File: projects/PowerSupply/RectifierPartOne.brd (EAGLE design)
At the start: 95 x 75 mm, 16 parts, among them K1 G2R2, X1 LINE-IN, X2 T1-PRI, X3 T1-SEC, X4 R1-OUT

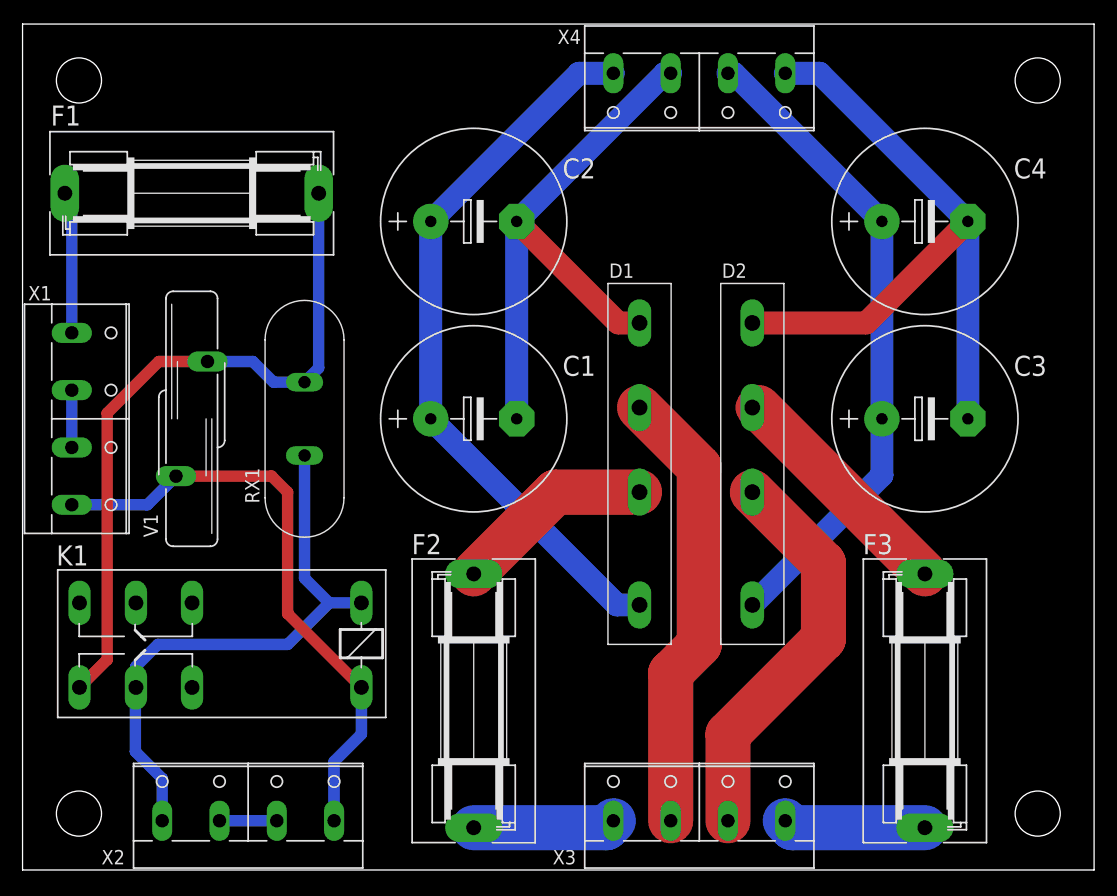
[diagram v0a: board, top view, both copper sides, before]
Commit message: feat: rectifier part one modified
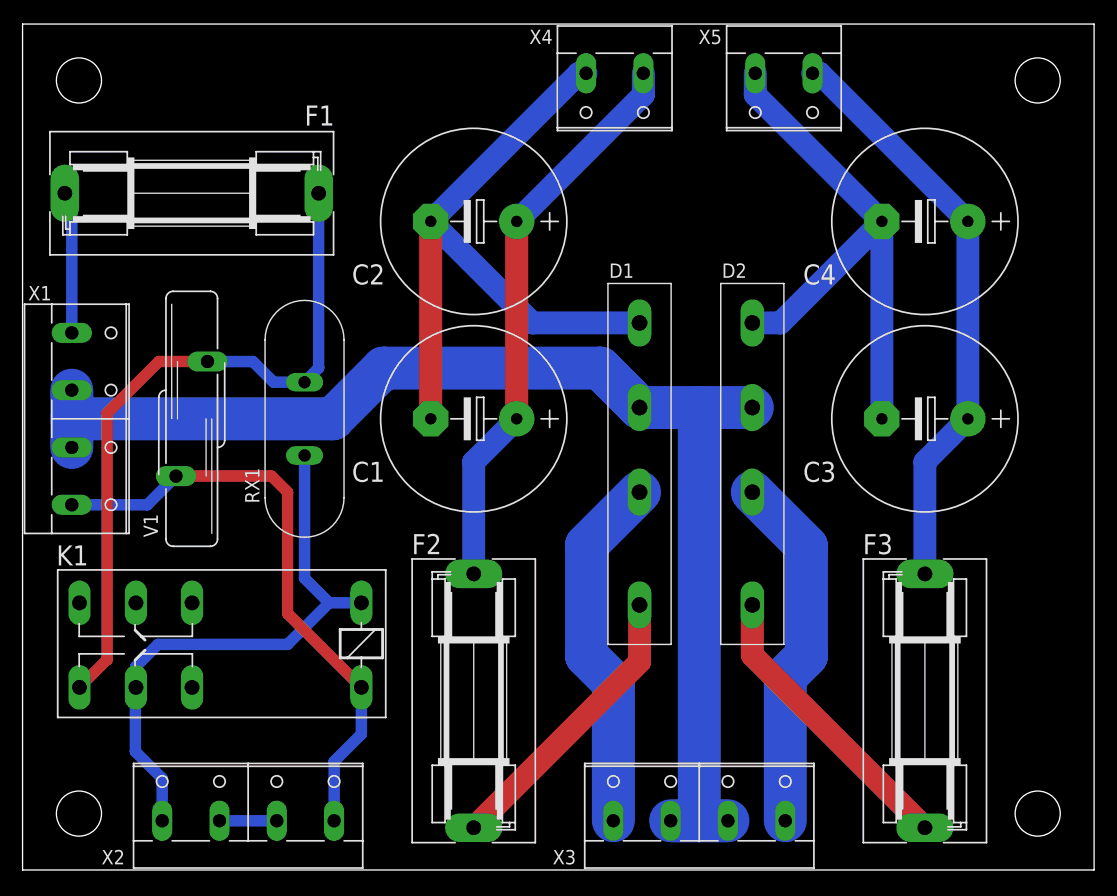
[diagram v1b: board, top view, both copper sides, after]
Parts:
- added X5: R1-5V, con-wago-508:W237-132
- C3, C4: value 2200µF -> 4700µF
- F2, F3: value 6.3AT -> 4A
- X4: value R1-OUT -> R1-12V; device con-wago-508:W237-4P -> con-wago-508:W237-132
- moved X4 7.50 mm to (52.5, 70.0)
- turned C1 to 180 degrees
- turned C2 to 180 degrees
- turned C3 to 180 degrees
- turned C4 to 180 degrees
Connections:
- removed net N$12: F3.1, X3.4
- removed net N$14: D2.VAC1, X3.3
- net N$1: now also D1.VAC1, X3.1; no longer D1.VAC2, X3.2
- net N$10: now also D1.+VDC, F2.1; no longer D1.VAC1, F2.2
- net N$11: now also D2.+VDC, F3.1; no longer D2.VAC2, F3.2
- net N$4: now also F2.2, X4.1; no longer D1.+VDC, X4.4
- net N$6: now also F3.2, X5.1; no longer D2.+VDC, X4.2
- net N$7: now also X4.2; no longer X4.3
- net N$8: now also D2.VAC1, X3.4; no longer F2.1, X3.1
- net N$9: now also X5.2; no longer X4.1
- net PE: now also D1.VAC2, D2.VAC2, X3.2, X3.3
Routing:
- net PE: track 5.08 -> 110.4 mm
- net N$14: track 35.2 -> 0.00 mm
- net N$8: track 12.6 -> 31.9 mm
- net N$4: track 64.5 -> 50.6 mm
- net N$12: track 12.6 -> 0.00 mm
- net N$9: track 62.0 -> 50.5 mm
- net N$10: track 17.7 -> 25.8 mm
- net N$1: track 39.9 -> 32.1 mm
- net N$7: track 51.2 -> 58.9 mm
- net N$6: track 57.9 -> 52.0 mm
- net N$11: track 21.4 -> 26.1 mm

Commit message: feat: rectifier parts modified
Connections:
- new net N$12: D1.VAC2, X3.2
- new net N$13: D2.VAC2, X3.3
- net PE: no longer D1.VAC2, D2.VAC2, X3.2, X3.3
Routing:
- net PE: track 110.4 -> 5.08 mm
- net N$13: track 0.00 -> 39.6 mm
- net N$12: track 0.00 -> 39.5 mm
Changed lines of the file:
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@@
 <contactref element="X1" pad="2"/>
 <contactref element="X1" pad="3"/>
-<contactref element="D1" pad="VAC2"/>
-<contactref element="D2" pad="VAC2"/>
-<contactref element="X3" pad="2"/>
-<contactref element="X3" pad="3"/>
-<wire x1="54.7" y1="41" x2="60" y2="41" width="3.81" layer="16"/>
-<wire x1="60" y1="41" x2="64.7" y2="41" width="3.81" layer="16"/>
-<wire x1="54.7" y1="41" x2="51.2" y2="44.5" width="3.81" layer="16"/>
-<wire x1="51.2" y1="44.5" x2="32" y2="44.5" width="3.81" layer="16"/>
-<wire x1="32" y1="44.5" x2="27.5" y2="40" width="3.81" layer="16"/>
-<wire x1="4.365" y1="37.46" x2="4.365" y2="40" width="3.81" layer="16"/>
-<wire x1="4.365" y1="40" x2="4.365" y2="42.54" width="3.81" layer="16"/>
-<wire x1="27.5" y1="40" x2="4.365" y2="40" width="3.81" layer="16"/>
-<wire x1="57.46" y1="4.365" x2="60" y2="4.365" width="3.81" layer="16"/>
-<wire x1="60" y1="4.365" x2="62.54" y2="4.365" width="3.81" layer="16"/>
-<wire x1="60" y1="4.365" x2="60" y2="41" width="3.81" layer="16"/>
+<wire x1="4.365" y1="37.46" x2="4.365" y2="42.54" width="1.016" layer="16"/>
 </signal>
 <signal name="+230VAC">
@@
 <wire x1="69.5" y1="28.7" x2="64.7" y2="33.5" width="3.81" layer="16"/>
 </signal>
+<signal name="N$12">
+<contactref element="D1" pad="VAC2"/>
+<contactref element="X3" pad="2"/>
+<wire x1="54.7" y1="41" x2="59.5" y2="36.2" width="3.81" layer="1"/>
+<wire x1="59.5" y1="36.2" x2="59.5" y2="18" width="3.81" layer="1"/>
+<wire x1="57.46" y1="15.96" x2="57.46" y2="4.365" width="3.81" layer="1"/>
+<wire x1="59.5" y1="18" x2="57.46" y2="15.96" width="3.81" layer="1"/>
+</signal>
+<signal name="N$13">
+<contactref element="D2" pad="VAC2"/>
+<contactref element="X3" pad="3"/>
+<wire x1="64.7" y1="41" x2="60" y2="36.3" width="3.81" layer="16"/>
+<wire x1="60" y1="36.3" x2="60" y2="18.5" width="3.81" layer="16"/>
+<wire x1="62.54" y1="15.96" x2="62.54" y2="4.365" width="3.81" layer="16"/>
+<wire x1="60" y1="18.5" x2="62.54" y2="15.96" width="3.81" layer="16"/>
+</signal>
 </signals>
